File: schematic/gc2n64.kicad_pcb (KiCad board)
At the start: 2 copper layers, 27.9 x 12.7 mm, 12 parts, among them U1 ATtiny85-20P

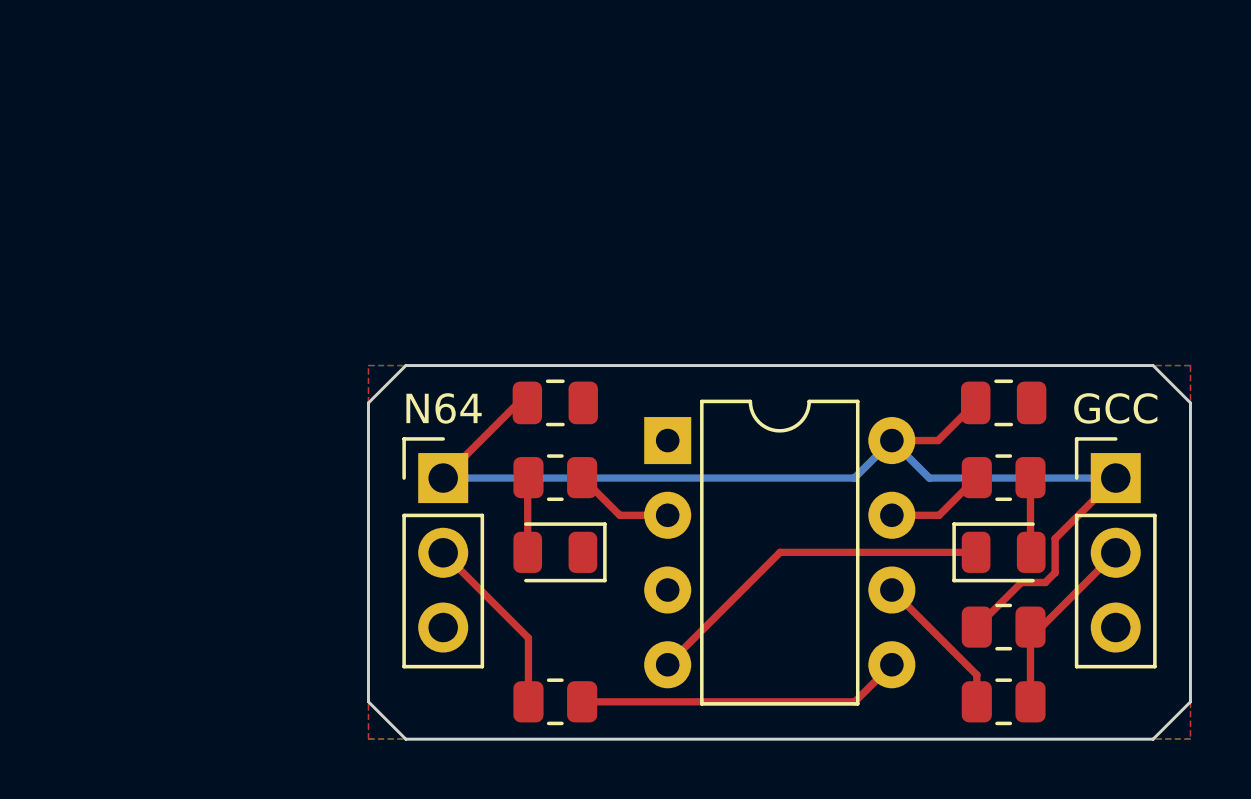
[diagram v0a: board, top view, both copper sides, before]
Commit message: feat(design): revision 2
Refactored the design to work with either attiny9 or attiny25, using a
basic hardware abstraction layer. So that the PCB can have a tagconnect
footprint rather than excessive through holes and plugging and
unplugging of attiny85 into a socket.
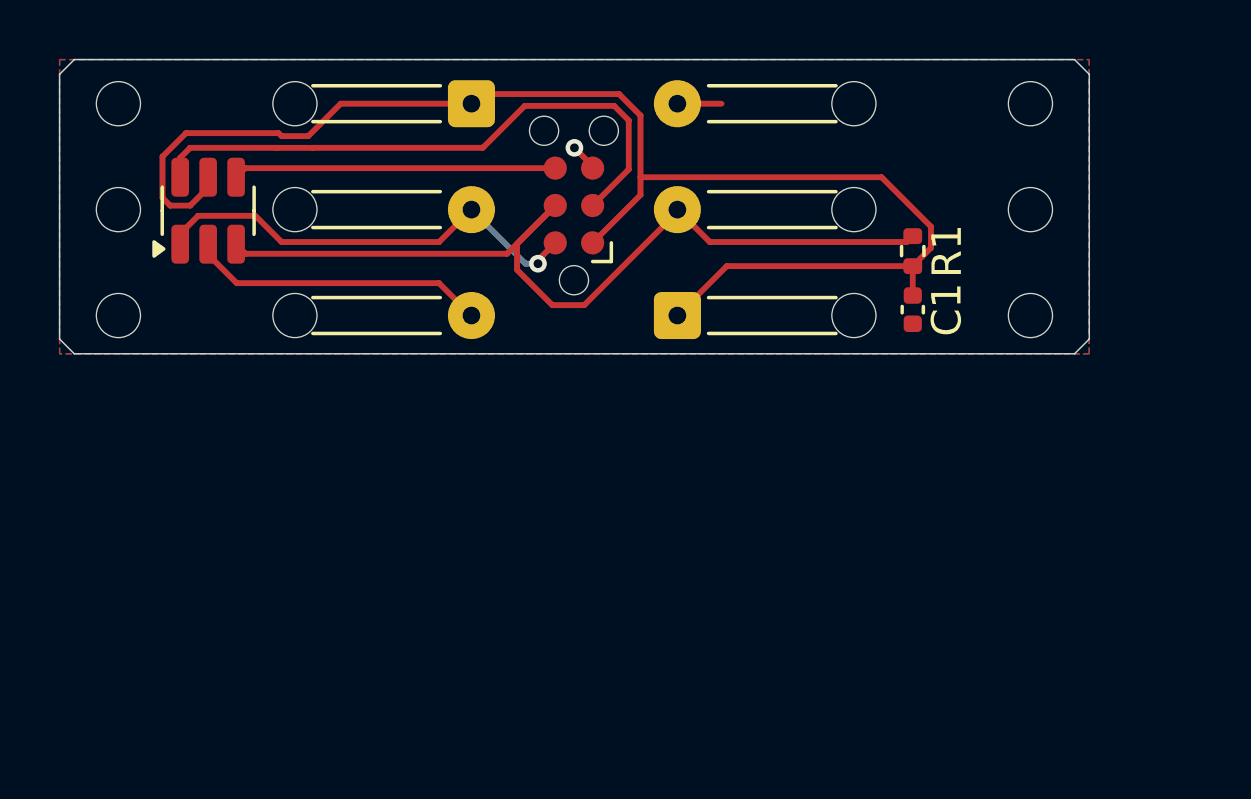
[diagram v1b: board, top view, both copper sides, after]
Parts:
- removed C2: 100nF, Capacitor_SMD:C_0805_2012Metric
- removed D1, D2: LED, LED_SMD:LED_0805_2012Metric
- removed GCC, N64: Conn_01x03, Connector_PinHeader_2.54mm:PinHeader_1x03_P2.54mm_Vertical
- removed R2: 22, Resistor_SMD:R_0805_2012Metric
- removed R3: 1K, Resistor_SMD:R_0805_2012Metric
- removed R4, R5: 470, Resistor_SMD:R_0805_2012Metric
- added J1: Conn_ARM_SWD_TagConnect_TC2030-NL, Connector:Tag-Connect_TC2030-IDC-NL_2x03_P1.27mm_Vertical, F.Cu at (32.4, 20.0)
- added J2: Conn_01x03, Connector_Wire:SolderWire-0.1sqmm_1x03_P3.6mm_D0.4mm_OD1mm_Relief2x, F.Cu at (28.9, 16.5)
- added J3: Conn_01x03, Connector_Wire:SolderWire-0.1sqmm_1x03_P3.6mm_D0.4mm_OD1mm_Relief2x, F.Cu at (35.9, 23.7)
- C1: value 10uF -> 100nF; footprint Capacitor_SMD:C_0805_2012Metric -> Capacitor_SMD:C_0402_1005Metric
- R1: value 22 -> 1K; footprint Resistor_SMD:R_0805_2012Metric -> Resistor_SMD:R_0402_1005Metric
- U1: value ATtiny85-20P -> ATtiny9-TS; footprint Package_DIP:DIP-8_W7.62mm -> Package_TO_SOT_SMD:SOT-23-6
- moved R1 19.6 mm to (43.9, 21.5), turned to -90 degrees
- moved U1 17.5 mm to (19.9, 20.1), turned to 90 degrees
- moved C1 12.6 mm to (43.9, 23.5), turned to -90 degrees
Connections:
- R1 pad 1: Net-(R1-Pad1) -> Net-(J1-SWCLK)
- R1 pad 2: Net-(J1-Pad2) -> +3V3
- U1 pad 1: unconnected-(U1-Pad1) -> Net-(J1-SWDIO)
- U1 pad 2: Net-(R5-Pad1) -> GND
- U1 pad 3: unconnected-(U1-Pad3) -> Net-(J1-SWCLK)
- U1 pad 4: GND -> Net-(J1-SWO)
- U1 pad 5: Net-(R1-Pad1) -> +3V3
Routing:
- net Net-(J1-SWCLK): track 0.00 -> 30.3 mm
- net Net-(J1-SWDIO): track 0.00 -> 15.3 mm, vias 0 -> 1
- net Net-(J1-~{RESET}): track 5.00 -> 20.2 mm
- net Net-(R1-Pad1): track 11.0 -> 0.00 mm
- net Net-(J1-SWO): track 0.00 -> 11.0 mm
- net +3V3: track 38.7 -> 48.1 mm
- net Net-(J2-Pad2): track 6.48 -> 0.00 mm
- net Net-(J1-Pad2): track 6.27 -> 0.00 mm
- net Net-(R5-Pad1): track 3.44 -> 0.00 mm
- net Net-(R4-Pad1): track 3.42 -> 0.00 mm
- net Net-(D2-Pad2): track 2.55 -> 0.00 mm
- net Net-(D1-Pad2): track 2.55 -> 0.00 mm
- net GND: track 12.1 -> 12.6 mm, vias 0 -> 1
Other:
- board size 27.9 x 12.7 mm -> 35 x 10 mm
